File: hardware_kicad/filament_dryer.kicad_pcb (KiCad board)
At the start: 2 copper layers, 43.8 x 51 mm, 60 parts, among them J1 grove_vert_holes, J2 USB_C_Receptacle_USB2.0, J3 grove_vert_holes, Q1 NMOS, U1 W25Q128JVS, U2 AMS1117-3.3, U3 RP2040, U4 DS18B20Z, U5 SHT31-DIS, U6 DS18B20Z, X1 12MHz Yangxing Tech X322512MS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

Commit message: Add dryer_print3d footprint and pcb
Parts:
- added REF**: dryer_print3d, 00_project_library:dryer_print3d, F.Cu at (0.00, 0.00)
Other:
- board size 43.8 x 51 mm -> 204.7 x 244.6 mm

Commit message: Added new parts
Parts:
- moved J3 232.3 mm to (361.5, 84.1)
- moved R3 232.3 mm to (383.7, 70.2)
- moved R4 232.3 mm to (377.2, 70.4)
- moved C1 232.3 mm to (374.0, 79.2)
- moved C11 232.3 mm to (358.0, 77.9)
- moved C12 232.3 mm to (358.8, 101.3)
- moved C17 232.3 mm to (379.1, 98.1)
- moved C18 232.3 mm to (381.1, 98.0)
- moved C20 232.3 mm to (381.6, 108.9)
- moved C3 232.3 mm to (381.6, 83.8)
- moved C6 232.3 mm to (361.6, 101.3)
- moved C9 232.3 mm to (382.9, 96.5)
- moved D3 232.3 mm to (367.9, 72.4)
- moved H1 232.3 mm to (373.0, 63.5)
- moved H2 232.3 mm to (373.0, 111.5)
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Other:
- board size 204.7 x 244.6 mm -> 336 x 130 mm
- board text added: "Fan Ambient"
- board text added: "Fan Silikagel"
- board text added: "H/T Ambient"
- board text added: "H/T Filament"
- board text added: "H/T Silicagel"
- board text added: "Persistaltic Pump"

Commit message: Some more layout
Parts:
- removed D3: POW_LED, LED_SMD:LED_0603_1608Metric
- removed JP1: Jumper_2_Bridged, Jumper:SolderJumper-2_P1.3mm_Open_RoundedPad1.0x1.5mm
- removed R8: 470R, Resistor_SMD:R_0402_1005Metric_Pad0.72x0.64mm_HandSolder
- removed R_POWER1: 120, Resistor_SMD:R_1206_3216Metric
- removed U4: DS18B20Z, Package_SO:SOIC-8_3.9x4.9mm_P1.27mm
- added C14: 10u, Capacitor_SMD:C_0603_1608Metric, F.Cu at (325.7, 102.2)
- added D1: HEATER_2, LED_SMD:LED_0603_1608Metric, F.Cu at (238.5, 128.5)
- added D4: 1N4148WS, Diode_SMD:D_SOD-323, F.Cu at (331.9, 88.0)
- added D5: 1N4148WS, Diode_SMD:D_SOD-323, F.Cu at (331.9, 91.0)
- added D6: FAN_1, LED_SMD:LED_0603_1608Metric, F.Cu at (304.3, 102.4)
- added D7: FAN_2, LED_SMD:LED_0603_1608Metric, F.Cu at (304.3, 105.0)
- added H5: MountingHole, MountingHole:MountingHole_3.2mm_M3, F.Cu at (121.0, 165.0)
- added J4: Peristatic Pump, 00_project_library:grove_vert_holes, F.Cu at (109.8, 100.0)
- added Q2: NMOS, Package_TO_SOT_SMD:SOT-23, F.Cu at (108.0, 119.0)
- added Q3: NMOS, Package_TO_SOT_SMD:SOT-23, F.Cu at (332.2, 79.9)
- added Q4: NMOS, Package_TO_SOT_SMD:SOT-23, F.Cu at (332.2, 84.3)
- added R17: 10k, Resistor_SMD:R_0402_1005Metric_Pad0.72x0.64mm_HandSolder, F.Cu at (322.1, 94.0)
- added R18: 10k, Resistor_SMD:R_0402_1005Metric_Pad0.72x0.64mm_HandSolder, F.Cu at (322.1, 96.0)
- added R19: 470R, Resistor_SMD:R_0402_1005Metric_Pad0.72x0.64mm_HandSolder, F.Cu at (322.1, 97.9)
- added R20: 470R, Resistor_SMD:R_0402_1005Metric_Pad0.72x0.64mm_HandSolder, F.Cu at (322.1, 99.9)
- added R22: 470R, Resistor_SMD:R_0402_1005Metric_Pad0.72x0.64mm_HandSolder, F.Cu at (322.1, 101.9)
- added R_POWER1_1: 120, Resistor_SMD:R_1206_3216Metric, F.Cu at (89.0, 122.2)
- added R_POWER1_10: 120, Resistor_SMD:R_1206_3216Metric, F.Cu at (96.5, 136.2)
- added R_POWER1_11: 120, Resistor_SMD:R_1206_3216Metric, F.Cu at (96.5, 140.9)
- added R_POWER1_12: 120, Resistor_SMD:R_1206_3216Metric, F.Cu at (96.5, 145.5)
- added R_POWER1_2: 120, Resistor_SMD:R_1206_3216Metric, F.Cu at (89.0, 126.8)
- added R_POWER1_3: 120, Resistor_SMD:R_1206_3216Metric, F.Cu at (89.0, 131.5)
- added R_POWER1_4: 120, Resistor_SMD:R_1206_3216Metric, F.Cu at (89.0, 136.2)
- added R_POWER1_5: 120, Resistor_SMD:R_1206_3216Metric, F.Cu at (89.0, 140.9)
- added R_POWER1_6: 120, Resistor_SMD:R_1206_3216Metric, F.Cu at (89.0, 145.5)
- added R_POWER1_7: 120, Resistor_SMD:R_1206_3216Metric, F.Cu at (96.5, 122.2)
- added R_POWER1_8: 120, Resistor_SMD:R_1206_3216Metric, F.Cu at (96.5, 126.8)
- added R_POWER1_9: 120, Resistor_SMD:R_1206_3216Metric, F.Cu at (96.5, 131.5)
- added R_POWER2_1: 120, Resistor_SMD:R_1206_3216Metric, F.Cu at (105.5, 122.2)
- added R_POWER2_10: 120, Resistor_SMD:R_1206_3216Metric, F.Cu at (112.3, 136.2)
- added R_POWER2_11: 120, Resistor_SMD:R_1206_3216Metric, F.Cu at (112.3, 140.9)
- added R_POWER2_12: 120, Resistor_SMD:R_1206_3216Metric, F.Cu at (112.4, 145.5)
- added R_POWER2_2: 120, Resistor_SMD:R_1206_3216Metric, F.Cu at (105.5, 126.8)
- added R_POWER2_3: 120, Resistor_SMD:R_1206_3216Metric, F.Cu at (105.5, 131.5)
- added R_POWER2_4: 120, Resistor_SMD:R_1206_3216Metric, F.Cu at (105.5, 136.2)
- added R_POWER2_5: 120, Resistor_SMD:R_1206_3216Metric, F.Cu at (105.5, 140.9)
- added R_POWER2_6: 120, Resistor_SMD:R_1206_3216Metric, F.Cu at (105.5, 145.5)
- added R_POWER2_7: 120, Resistor_SMD:R_1206_3216Metric, F.Cu at (112.3, 122.2)
- added R_POWER2_8: 120, Resistor_SMD:R_1206_3216Metric, F.Cu at (112.3, 126.8)
- added R_POWER2_9: 120, Resistor_SMD:R_1206_3216Metric, F.Cu at (112.3, 131.5)
- added TP10: FAN_SILICAGEL_BLACK, TestPoint:TestPoint_Pad_D3.0mm, F.Cu at (58.2, 157.5)
- added TP11: HT_SILICAGEL_SCL, TestPoint:TestPoint_Pad_D3.0mm, F.Cu at (129.3, 127.5)
- added TP6: HT_SILICAGEL_SCA, TestPoint:TestPoint_Pad_D3.0mm, F.Cu at (129.5, 132.6)
- added TP8: FAN_AMBIENT_BLACK, TestPoint:TestPoint_Pad_D3.0mm, F.Cu at (129.5, 154.7)
- added TP9: FAN_SILICAGEL_RED, TestPoint:TestPoint_Pad_D3.0mm, F.Cu at (58.2, 162.1)
- D2: value HEATING_LED -> HEATER_1
- H1, H2, H3, H4: footprint MountingHole:MountingHole_2.2mm_M2 -> MountingHole:MountingHole_3.2mm_M3
- J1: value grove_vert_holes -> USB_C_Receptacle_USB2.0; footprint 00_project_library:grove_vert_holes -> 00_project_library:USB_C_Receptacle_Palconn_UTC16-G
- J2: value USB_C_Receptacle_USB2.0 -> H/T Ambient; footprint 00_project_library:USB_C_Receptacle_Palconn_UTC16-G -> 00_project_library:grove_vert_holes
- J3: value grove_vert_holes -> T Aux
- R11: value 10k -> 470R
- TP2: value TestPoint -> HT_SILICAGEL_GND; footprint TestPoint:TestPoint_Pad_D1.5mm -> TestPoint:TestPoint_Pad_D3.0mm
- TP3: value TestPoint -> HT_SILICAGEL_3V3; footprint TestPoint:TestPoint_Pad_D1.5mm -> TestPoint:TestPoint_Pad_D3.0mm
- TP4, TP5: footprint TestPoint:TestPoint_Pad_D2.5mm -> TestPoint:TestPoint_Pad_D1.5mm
- TP7: value TestPoint -> FAN_AMBIENT_RED; footprint TestPoint:TestPoint_Pad_D1.0mm -> TestPoint:TestPoint_Pad_D3.0mm
- U5: value SHT31-DIS -> H/T Filament
- moved H3 314.0 mm to (72.0, 114.0)
- moved H1 309.1 mm to (81.0, 165.0)
- moved H2 303.5 mm to (72.0, 150.0)
- moved J2 298.6 mm to (82.8, 100.1), turned to 90 degrees
- moved SW_RESET1 289.5 mm to (63.0, 52.1), turned to 90 degrees
- moved R3 281.9 mm to (102.5, 49.4), turned to -90 degrees
- moved C13 280.5 mm to (93.1, 51.7)
- moved C1 279.1 mm to (95.6, 59.4)
- moved C10 279.1 mm to (106.7, 68.4)
- moved C15 279.1 mm to (94.9, 71.4)
- moved C17 279.1 mm to (100.7, 78.3)
- moved C18 279.1 mm to (102.7, 78.3)
- moved C2 279.1 mm to (105.8, 76.7)
- moved C3 279.1 mm to (103.2, 64.0)
- moved C4 279.1 mm to (102.2, 64.0)
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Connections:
- net /TEMP_GROVE_1WIRE renamed /T_AUX_1WIRE
- net /TEMP_HEATING_1WIRE renamed /T_HEATING_1WIRE
- D2 pad 1: /GPIO_HEATER -> /GPIO_HEATER_1
- Q1 pad 2: /GPIO_HEATER -> /GPIO_HEATER_1
- R11 pad 1: Net-(U5-ADDR) -> Net-(D1-A)
- R13 pad 2: /HUMIDITY_SDA -> /HT_FILAMENT_SDA
- R14 pad 2: /HUMIDITY_SCL -> /HT_FILAMENT_SCL
- R15 pad 2: /TEMP_BOARD_1WIRE -> /T_BOARD_1WIRE
- R3 pad 1: Net-(J2-CC1) -> Net-(J1-CC1)
- R4 pad 1: Net-(J2-CC2) -> Net-(J1-CC2)
- TP2 pad 1: /HUMIDITY_SDA -> GND
- TP3 pad 1: /HUMIDITY_SCL -> +3V3
- TP4 pad 1: /TEMP_BOARD_1WIRE -> /T_BOARD_1WIRE
- TP7 pad 1: Net-(C18-Pad1) -> +5V
- U3 pad 12: /GPIO_HEATER -> /T_BOARD_1WIRE
- U3 pad 13: /HUMIDITY_SDA -> /HT_GROVE_SDA
- U3 pad 14: /HUMIDITY_SCL -> /HT_GROVE_SCL
- U3 pad 16: unconnected-(U3-GPIO13-Pad16) -> /GPIO_HEATER_1
- U3 pad 17: unconnected-(U3-GPIO14-Pad17) -> /GPIO_HEATER_2
- U3 pad 2: /TEMP_BOARD_1WIRE -> /T_BOARD_1WIRE
- U3 pad 27: unconnected-(U3-GPIO16-Pad27) -> /GPIO_PUMP_STEP
- U3 pad 29: unconnected-(U3-GPIO18-Pad29) -> /HT_FILAMENT_SDA
- U3 pad 30: unconnected-(U3-GPIO19-Pad30) -> /HT_FILAMENT_SCL
- U3 pad 6: /HUMIDITY_GROVE_SDA -> /HT_GROVE_SDA
- U3 pad 7: /HUMIDITY_GROVE_SCL -> /HT_GROVE_SCL
- U5 pad 1: /HUMIDITY_SDA -> /HT_FILAMENT_SDA
- U5 pad 2: Net-(U5-ADDR) -> GND
- U5 pad 4: /HUMIDITY_SCL -> /HT_FILAMENT_SCL
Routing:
- net +5V: track 97.4 -> 412.6 mm
- net +3V3: track 163.9 -> 107.0 mm
- net Net-(Q2-D): track 0.00 -> 53.0 mm
- net /RUN: track 56.4 -> 5.24 mm, vias 2 -> 0
- net Net-(Q1-D): track 5.57 -> 54.7 mm
- net /TEMP_BOARD_1WIRE: track 32.0 -> 0.00 mm, vias 2 -> 0
- net /QSPI_SS: track 51.0 -> 21.4 mm, vias 2 -> 0
- net /GPIO_HEATER: track 27.6 -> 0.00 mm
- net /HUMIDITY_SCL: track 25.9 -> 0.00 mm
- net /HUMIDITY_SDA: track 22.5 -> 0.00 mm
- net /T_AUX_1WIRE: track 22.4 -> 0.00 mm
- net /HUMIDITY_GROVE_SDA: track 18.9 -> 0.00 mm
- net /T_HEATING_1WIRE: track 26.0 -> 11.0 mm
- net /HUMIDITY_GROVE_SCL: track 14.9 -> 0.00 mm
- net GND: track 22.5 -> 11.4 mm, vias 67 -> 8
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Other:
- board size 336 x 130 mm -> 94 x 130 mm
- board text removed: "${TITLE}"
- board text removed: "Fan Ambient"
- board text removed: "Fan Silikagel"
- board text removed: "H/T Ambient"
- board text removed: "H/T Filament"
- board text removed: "H/T Silicagel"
- board text removed: "HUMIDITY_BOARD"
- board text removed: "Persistaltic Pump"
- board text removed: "TEMP_BOARD"

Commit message: tmp
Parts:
- added D3: POW_LED, LED_SMD:LED_0603_1608Metric, F.Cu at (186.5, 96.1)
- added R8: 470R, Resistor_SMD:R_0402_1005Metric_Pad0.72x0.64mm_HandSolder, F.Cu at (190.2, 95.8)
- added U4: DS18B20Z, Package_SO:SOIC-8_3.9x4.9mm_P1.27mm, F.Cu at (101.1, 134.1)
- moved R15 262.4 mm to (95.6, 74.0)
- moved Q2 1.71 mm to (109.7, 119.0)
- moved R_POWER2_10 1.40 mm to (113.7, 136.2)
- moved R_POWER2_11 1.40 mm to (113.7, 140.9)
- moved R_POWER2_8 1.40 mm to (113.7, 126.9)
- moved R_POWER2_9 1.40 mm to (113.7, 131.5)
- moved R_POWER2_1 1.40 mm to (106.9, 122.2)
- moved R_POWER2_12 1.40 mm to (113.8, 145.6)
- moved R_POWER2_2 1.40 mm to (106.9, 126.8)
- moved R_POWER2_3 1.40 mm to (106.9, 131.5)
- moved R_POWER2_4 1.40 mm to (106.9, 136.2)
- moved R_POWER2_5 1.40 mm to (106.9, 140.9)
- moved R_POWER2_6 1.40 mm to (106.9, 145.5)
- moved R_POWER2_7 1.40 mm to (113.7, 122.2)
- moved Q1 0.95 mm to (92.8, 118.7)
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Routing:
- net +3V3: track 107.0 -> 274.9 mm, vias 6 -> 9
- net /T_BOARD_1WIRE: track 6.84 -> 84.4 mm, vias 0 -> 2
- net +5V: track 412.6 -> 394.9 mm
- net GND: vias 8 -> 9

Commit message: Update 3d footprint
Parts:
- removed REF**: dryer_print3d, 00_project_library:dryer_print3d
- removed TP4: TestPoint, TestPoint:TestPoint_Pad_D1.5mm
- added dryer_print3D1: dryer_print3D, 00_project_library:dryer_print3d, F.Cu at (101.0, 170.0)

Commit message: routing
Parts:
- removed R1: 4k7, Resistor_SMD:R_0402_1005Metric_Pad0.72x0.64mm_HandSolder
- removed R17, R18: 10k, Resistor_SMD:R_0402_1005Metric_Pad0.72x0.64mm_HandSolder
- removed TP5: TestPoint, TestPoint:TestPoint_Pad_D1.5mm
- removed U6: DS18B20Z, Package_SO:SOIC-8_3.9x4.9mm_P1.27mm
- moved TP1 398.1 mm to (-33.3, 41.1)
- moved Q4 283.3 mm to (57.2, 152.4), turned to 180 degrees
- moved D5 277.8 mm to (63.0, 160.5), turned to 90 degrees
- moved R20 267.5 mm to (58.4, 145.0), turned to 90 degrees
- moved R13 262.2 mm to (128.3, 51.6), turned to -90 degrees
- moved C20 251.0 mm to (136.5, 54.5)
- moved R12 251.0 mm to (140.5, 49.9), turned to 90 degrees
- moved D7 249.7 mm to (58.4, 148.3), turned to 90 degrees
- moved R14 247.7 mm to (134.8, 54.3), turned to -90 degrees
- moved Q3 217.9 mm to (125.7, 149.4), turned to 180 degrees
- moved D4 216.6 mm to (125.5, 153.4), turned to 90 degrees
- moved R22 214.0 mm to (108.4, 89.7), turned to -90 degrees
- moved R19 188.3 mm to (142.2, 153.9)
- moved D6 173.2 mm to (138.9, 153.9)
- moved R11 163.4 mm to (77.1, 89.3)
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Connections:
- R13 pad 2: /HT_FILAMENT_SDA -> /HT_BOARD_SDA
- R14 pad 2: /HT_FILAMENT_SCL -> /HT_BOARD_SCL
- R15 pad 2: /T_BOARD_1WIRE -> /T_HEATING_1WIRE
- TP11 pad 1: /HT_SILICAGEL_SCL -> /HT_BOARD_SCL
- TP6 pad 1: /HT_SILICAGEL_SDA -> /HT_BOARD_SDA
- U3 pad 11: /T_HEATING_1WIRE -> unconnected-(U3-GPIO8-Pad11)
- U3 pad 18: unconnected-(U3-GPIO15-Pad18) -> /T_HEATING_1WIRE
- U3 pad 29: /HT_FILAMENT_SDA -> unconnected-(U3-GPIO18-Pad29)
- U3 pad 30: /HT_FILAMENT_SCL -> unconnected-(U3-GPIO19-Pad30)
- U3 pad 32: unconnected-(U3-GPIO21-Pad32) -> /GPIO_FAN_AMBIENT
- U3 pad 38: unconnected-(U3-GPIO26/ADC0-Pad38) -> /HT_BOARD_SDA
- U3 pad 39: unconnected-(U3-GPIO27/ADC1-Pad39) -> /HT_BOARD_SCL
- U4 pad 4: /T_BOARD_1WIRE -> /T_HEATING_1WIRE
- U5 pad 1: /HT_FILAMENT_SDA -> /HT_BOARD_SDA
- U5 pad 2: GND -> +3V3
- U5 pad 4: /HT_FILAMENT_SCL -> /HT_BOARD_SCL
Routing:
- net /GPIO_HEATER_2: track 0.00 -> 122.0 mm, vias 0 -> 2
- net /HT_BOARD_SCL: track 0.00 -> 117.2 mm, vias 0 -> 4
- net /HT_BOARD_SDA: track 0.00 -> 107.3 mm, vias 0 -> 3
- net /GPIO_FAN_AMBIENT: track 0.00 -> 102.7 mm, vias 0 -> 2
- net /T_BOARD_1WIRE: track 84.4 -> 0.00 mm, vias 2 -> 0
- net /T_HEATING_1WIRE: track 11.0 -> 76.6 mm, vias 0 -> 2
- net +3V3: track 274.9 -> 334.2 mm, vias 9 -> 12
- net +5V: track 394.9 -> 358.0 mm
- net GND: track 11.4 -> 41.1 mm, vias 9 -> 23
- net /GPIO_HEATER_1: track 0.00 -> 22.8 mm
- net /GPIO_PUMP_STEP: track 0.00 -> 18.5 mm
- net Net-(J4-Pad1): track 0.00 -> 11.2 mm, vias 0 -> 2
- net Net-(D5-A): track 0.00 -> 9.71 mm
- net Net-(D4-A): track 0.00 -> 6.78 mm
- net Net-(D3-K): track 0.00 -> 2.91 mm
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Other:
- board text removed: "BOOT"
- board text removed: "HUMIDITY I2C"
- board text removed: "RESET"
- board text removed: "TEMP 1WIRE"
- board text removed: "TEMP_HEATER"

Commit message: 2023-08-20 review schematics
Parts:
- moved R16 153.5 mm to (92.1, 99.4), turned to -90 degrees
- moved C14 132.5 mm to (133.9, 145.3)
- moved TP1 119.0 mm to (84.4, 59.1)
- moved C12 94.8 mm to (153.5, 81.3)
- moved C6 94.8 mm to (156.3, 81.3)
- moved C11 84.3 mm to (156.8, 51.4)
- moved D4 3.58 mm to (128.4, 155.5)
- moved Q3 2.00 mm to (127.4, 150.4)
- moved TP7 1.74 mm to (131.3, 159.5)
- moved TP8 1.74 mm to (131.3, 154.2)
- moved D6 0.71 mm to (139.0, 153.2)
- moved R19 0.71 mm to (142.3, 153.2)
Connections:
- U3 pad 15: unconnected-(U3-GPIO12-Pad15) -> /T_AUX_1WIRE
- U3 pad 4: /T_AUX_1WIRE -> unconnected-(U3-GPIO2-Pad4)
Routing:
- net /RUN: track 5.24 -> 58.4 mm, vias 0 -> 2
- net /T_AUX_1WIRE: track 0.00 -> 33.2 mm, vias 0 -> 2
- net GND: track 41.1 -> 63.5 mm, vias 23 -> 27
- net /QSPI_SS: track 21.4 -> 38.3 mm
- net +3V3: track 334.2 -> 340.6 mm
- net Net-(D4-A): track 6.78 -> 5.95 mm
- net +5V: track 358.0 -> 358.7 mm

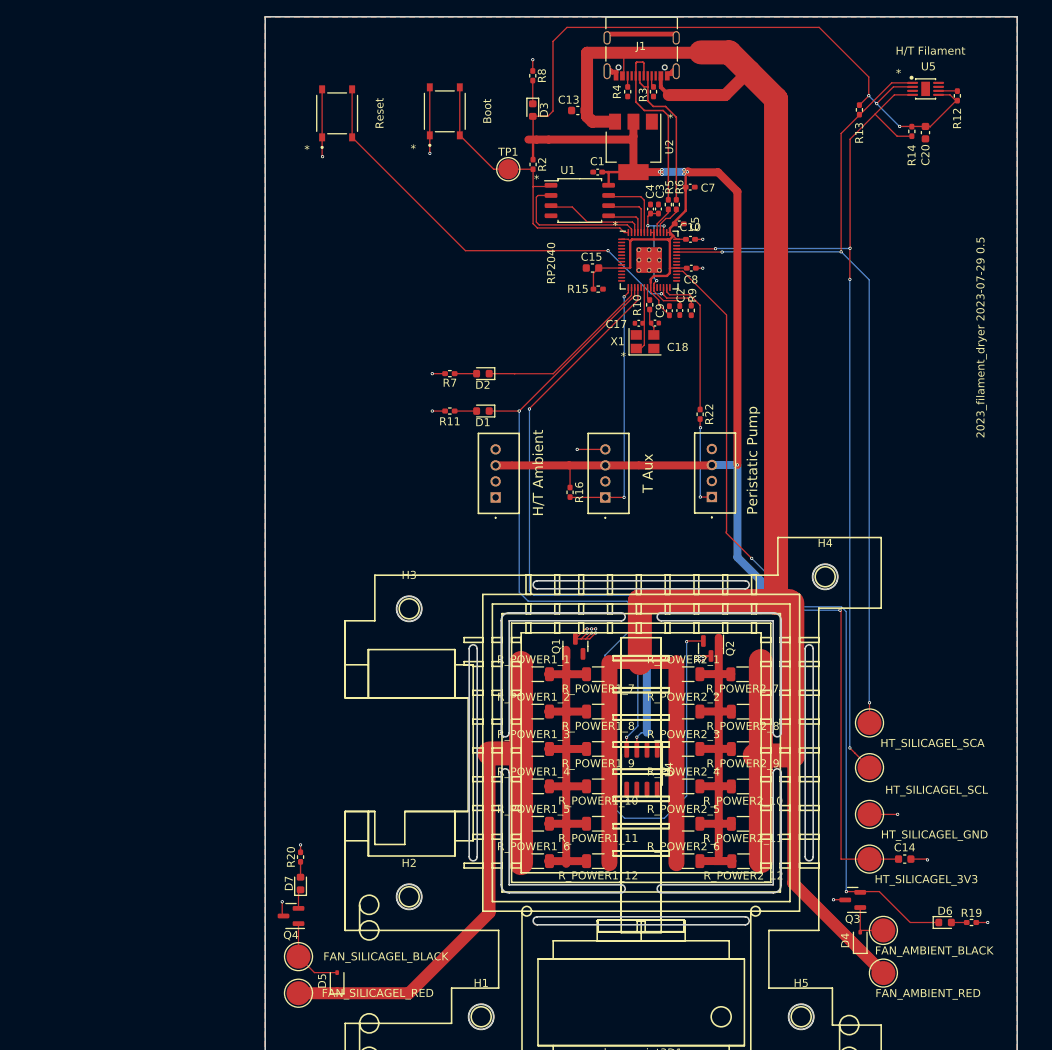
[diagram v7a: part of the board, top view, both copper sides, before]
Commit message: Removed resistors, add locked zones
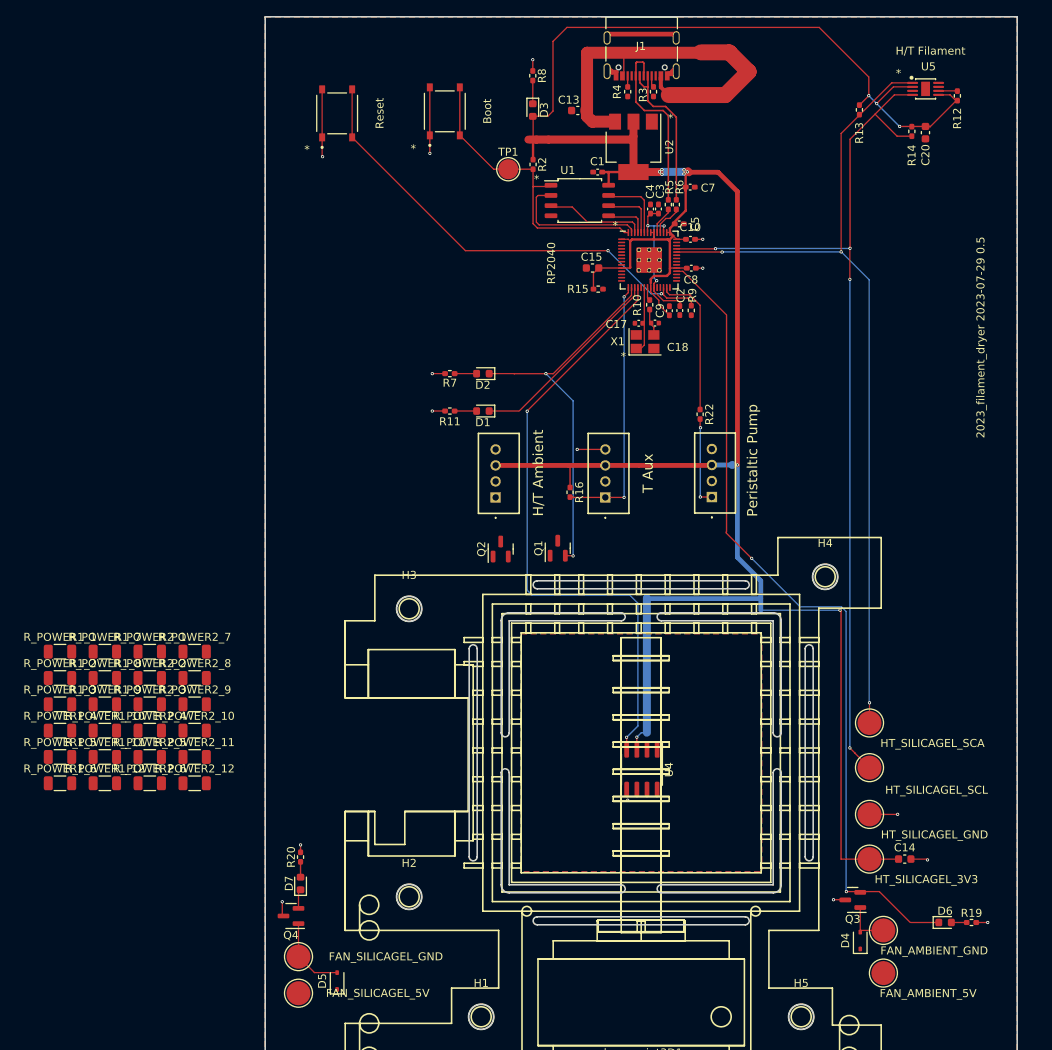
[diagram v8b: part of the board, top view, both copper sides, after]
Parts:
- J4: value Peristatic Pump -> Peristaltic Pump
- TP10: value FAN_SILICAGEL_BLACK -> FAN_SILICAGEL_GND
- TP7: value FAN_AMBIENT_RED -> FAN_AMBIENT_5V
- TP8: value FAN_AMBIENT_BLACK -> FAN_AMBIENT_GND
- TP9: value FAN_SILICAGEL_RED -> FAN_SILICAGEL_5V
- moved R_POWER2_12 69.3 mm to (45.2, 135.8), turned to 0 degrees
- moved R_POWER2_11 69.1 mm to (45.2, 132.5), turned to 0 degrees
- moved R_POWER2_10 68.9 mm to (45.2, 129.2), turned to 0 degrees
- moved R_POWER2_9 68.8 mm to (45.2, 125.9), turned to 0 degrees
- moved R_POWER2_8 68.7 mm to (45.2, 122.7), turned to 0 degrees
- moved R_POWER2_7 68.5 mm to (45.2, 119.4), turned to 0 degrees
- moved R_POWER2_6 68.0 mm to (39.6, 135.8)
- moved R_POWER2_5 67.8 mm to (39.6, 132.5)
- moved R_POWER2_4 67.7 mm to (39.6, 129.2)
- moved R_POWER2_3 67.5 mm to (39.6, 125.9)
- moved R_POWER2_2 67.4 mm to (39.6, 122.7)
- moved R_POWER2_1 67.4 mm to (39.6, 119.4)
- moved R_POWER1_12 62.4 mm to (34.0, 135.8), turned to 0 degrees
- moved R_POWER1_11 62.2 mm to (34.0, 132.5), turned to 0 degrees
- moved R_POWER1_10 62.1 mm to (34.0, 129.2), turned to 0 degrees
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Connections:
- D1 pad 1: /GPIO_HEATER_2 -> Net-(D1-K)
- D1 pad 2: Net-(D1-A) -> +5V
- D2 pad 1: /GPIO_HEATER_1 -> Net-(D2-K)
- D2 pad 2: Net-(D2-A) -> +5V
- D6 pad 1: /GPIO_FAN_AMBIENT -> Net-(D6-K)
- D6 pad 2: Net-(D6-A) -> /GPIO_FAN_AMBIENT
- D7 pad 1: /GPIO_FAN_SILICAGEL -> Net-(D7-K)
- D7 pad 2: Net-(D7-A) -> /GPIO_FAN_SILICAGEL
- R11 pad 1: Net-(D1-A) -> Net-(D1-K)
- R11 pad 2: GND -> Net-(Q2-D)
- R19 pad 1: Net-(D6-A) -> Net-(D6-K)
- R20 pad 1: Net-(D7-A) -> Net-(D7-K)
- R7 pad 1: Net-(D2-A) -> Net-(D2-K)
- R7 pad 2: GND -> Net-(Q1-D)
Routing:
- net +5V: track 358.7 -> 54.6 mm
- net /GPIO_HEATER_2: track 122.0 -> 25.1 mm, vias 2 -> 0
- net Net-(Q1-D): track 54.6 -> 1.60 mm, vias 0 -> 1
- net Net-(Q2-D): track 53.0 -> 1.60 mm, vias 0 -> 1
- net /GPIO_HEATER_1: track 22.8 -> 48.0 mm, vias 0 -> 2
- net GND: track 63.5 -> 45.7 mm, vias 27 -> 13
- net Net-(D2-A): track 2.74 -> 0.00 mm
- net Net-(D1-A): track 2.74 -> 0.00 mm
- net Net-(D7-A): track 1.92 -> 0.00 mm
- net Net-(D6-A): track 1.92 -> 0.00 mm
- net /GPIO_FAN_SILICAGEL: track 2.07 -> 3.99 mm
- net /GPIO_FAN_AMBIENT: track 102.9 -> 104.9 mm
- net +3V3: track 340.6 -> 339.4 mm
